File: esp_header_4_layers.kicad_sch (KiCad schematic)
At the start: 28 parts, among them J10 BM05B-SRSS, J11 BM05B-SRSS, J12 BM05B-SRSS, J2 JST_VH_B2P, J6 BM02B-SRSS-TB, J7 B3B-EH-A, J8 B3B-EH-A, J9 B3B-EH-A, Q1 AOD472A, SW1 SW_DIP_x01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

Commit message: untracked unnecessary files
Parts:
- J10, J11, J12: JLCPCB Part# (none) -> C160391
- J6: JLCPCB Part# (none) -> C160388
- Q1: value AOD472A -> MS50N06; JLCPCB Part# (none) -> C2902884
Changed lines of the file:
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@@
 			)
 		)
-		(property "JLCPCB Part#" ""
+		(property "JLCPCB Part#" "C160391"
 			(at 140.97 36.83 0)
 			(hide yes)
@@
 			)
 		)
-		(property "JLCPCB Part#" ""
+		(property "JLCPCB Part#" "C160391"
 			(at 140.97 72.39 0)
 			(hide yes)
@@
 			)
 		)
-		(property "JLCPCB Part#" ""
+		(property "JLCPCB Part#" "C160388"
 			(at 158.75 97.79 0)
 			(hide yes)
@@
 			)
 		)
-		(property "JLCPCB Part#" ""
+		(property "JLCPCB Part#" "C160391"
 			(at 140.97 54.61 0)
 			(hide yes)
@@
 			)
 		)
-		(property "Value" "AOD472A"
+		(property "Value" "MS50N06"
 			(at 44.45 149.8599 0)
 			(show_name no)
@@
 			)
 		)
-		(property "JLCPCB Part#" ""
+		(property "JLCPCB Part#" "C2902884"
 			(at 38.1 148.59 0)
 			(hide yes)

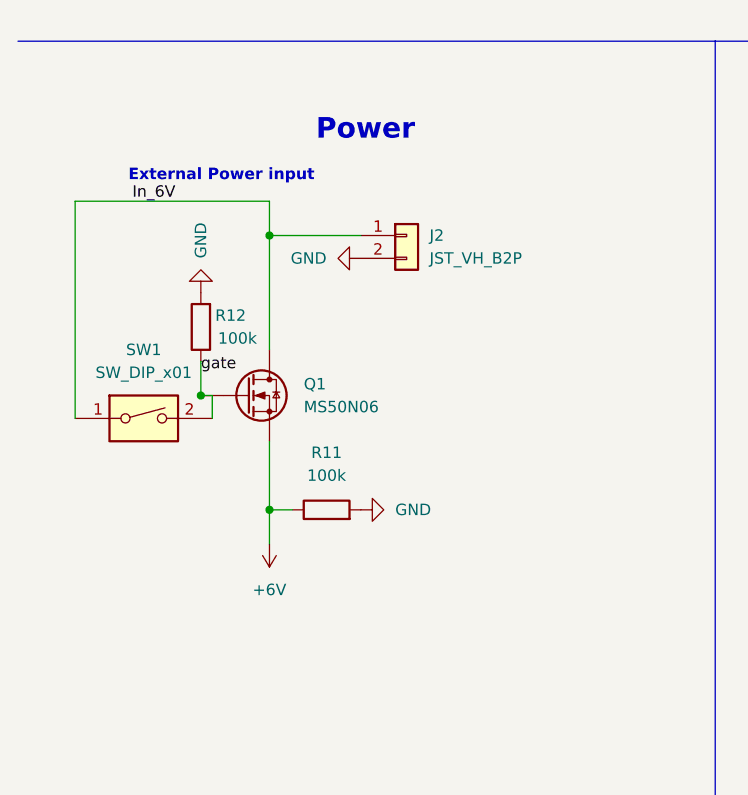
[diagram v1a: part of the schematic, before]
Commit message: made schematic clearer
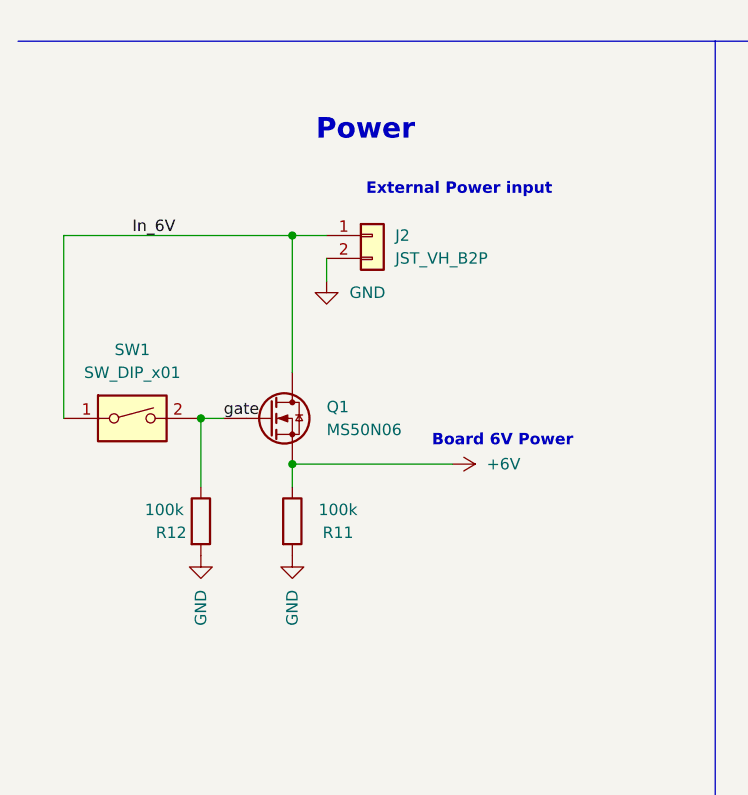
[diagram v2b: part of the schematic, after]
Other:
- note added: "Board 6V Power"
- moved on the sheet: J2, Q1, R11, R12, SW1

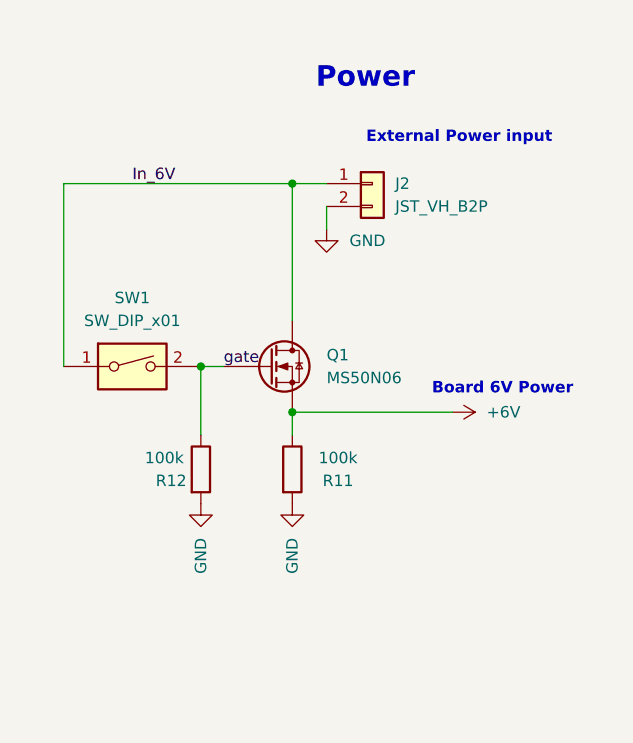
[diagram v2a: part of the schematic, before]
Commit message: changed to PMOS instead of NMOS
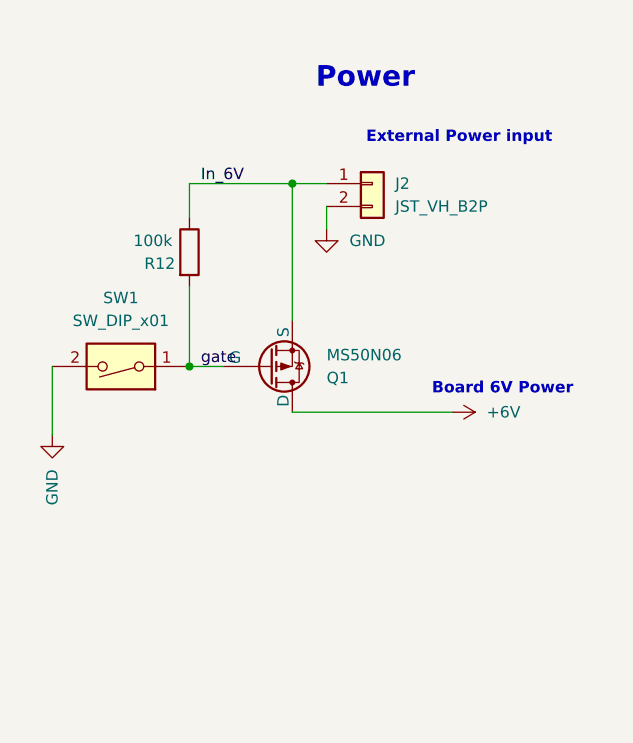
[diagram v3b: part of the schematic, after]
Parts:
- removed R11: 100k, Resistor_SMD:R_0603_1608Metric, symbol Device:R
- Q1: symbol Device:Q_NMOS -> Simulation_SPICE:PMOS
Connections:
- net +6V: now also Q1.D; no longer Q1.S
- net GND: now also SW1.2; no longer R12.2
- net In_6V: now also Q1.S, R12.1; no longer Q1.D, SW1.1
- net gate: now also R12.2, SW1.1; no longer R12.1, SW1.2
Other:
- moved on the sheet: SW1

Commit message: added model for pmos
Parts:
- Q1: value MS50N06 -> HY19P03D; JLCPCB Part# C2902884 -> C122492
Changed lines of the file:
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@@
 			)
 		)
-		(property "Value" "MS50N06"
+		(property "Value" "HY19P03D"
 			(at 46.99 149.8601 0)
 			(show_name no)
@@
 			)
 		)
-		(property "JLCPCB Part#" "C2902884"
+		(property "JLCPCB Part#" "C122492"
 			(at 40.64 151.13 0)
 			(hide yes)
